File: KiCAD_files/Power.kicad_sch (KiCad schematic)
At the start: 44 parts, among them J101 Wago 6 contacts, P101 Power2, U101 AMC1311, U102 MCP6486UT-E/LT, U103 MCP6486UT-E/LT, U104 ACS723LLCTR-20AB

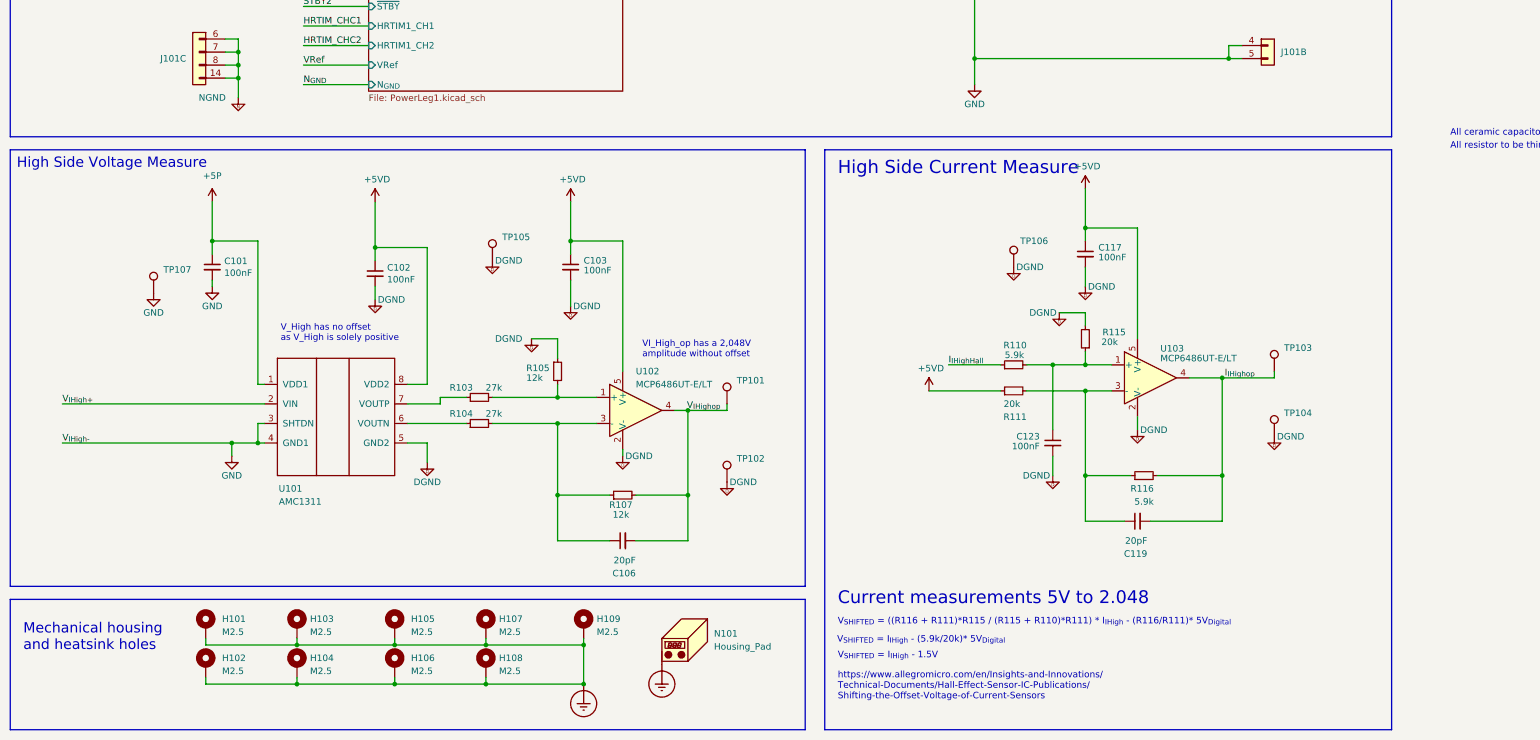
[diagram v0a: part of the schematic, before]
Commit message: better comments for VHigh conditionning signal
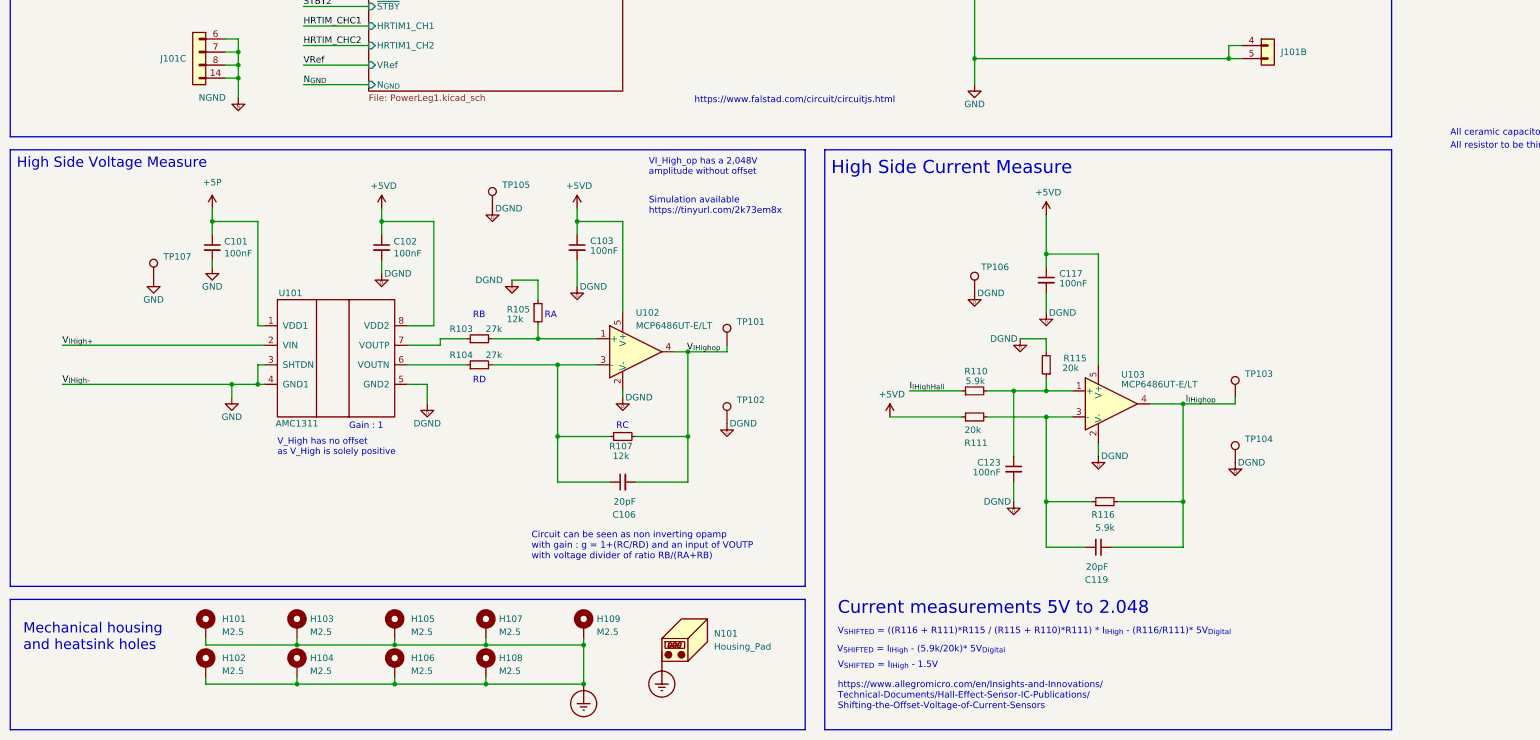
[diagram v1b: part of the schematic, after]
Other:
- note added: "Circuit can be seen as non inverting opamp with gain : g = 1+(RC/RD) and an input of VOUTP with voltage divider of ratio RB/(RA+RB)"
- note added: "Gain : 1"
- note added: "RA"
- note added: "RB"
- note added: "RC"
- note added: "RD"
- note added: "Simulation available https://tinyurl.com/2k73em8x"
- note added: "https://www.falstad.com/circuit/circuitjs.html"
- moved on the sheet: C101, C102, C103, C106, C117, C119, C123, R103, R104, R105, R107, R110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

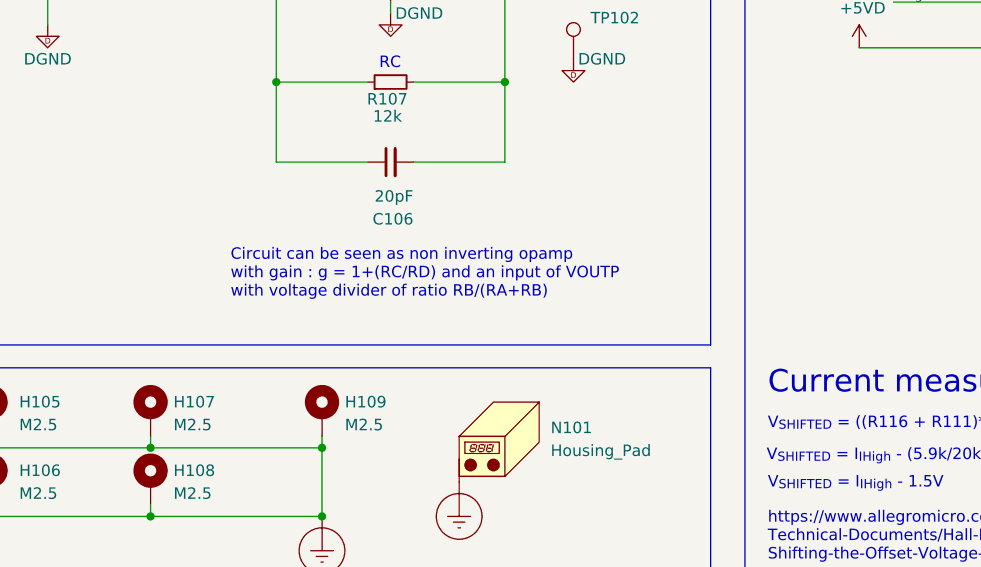
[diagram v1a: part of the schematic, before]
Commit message: more details for VLow conditionning
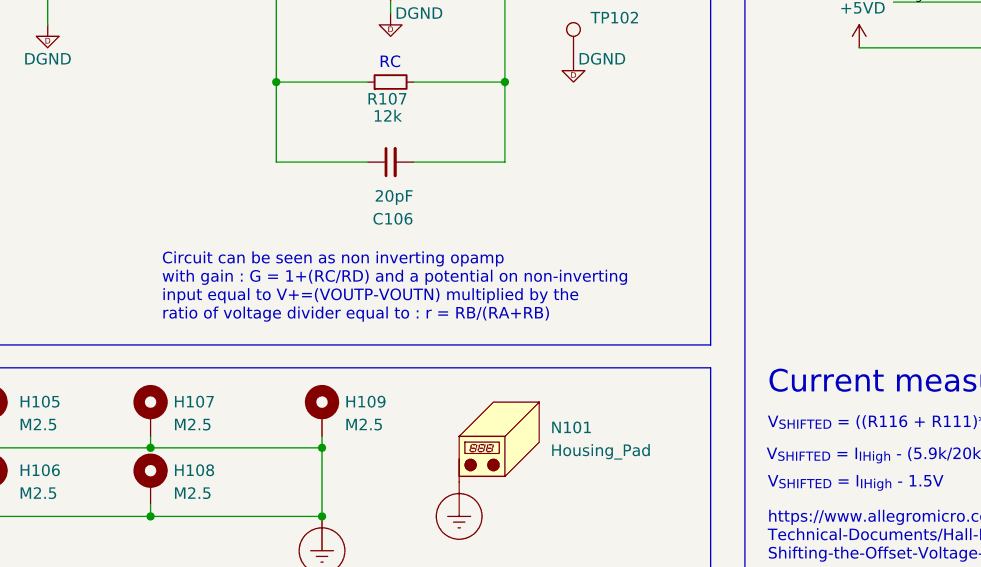
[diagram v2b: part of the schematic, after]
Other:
- note added: "Circuit can be seen as non inverting opamp with gain : G = 1+(RC/RD) and a potential on non-inverting input equal to V+=(VOUTP-VOUTN) multiplied by the ratio of voltage divider equal to : r = RB/(RA+RB)"
- note removed: "Circuit can be seen as non inverting opamp with gain : g = 1+(RC/RD) and an input of VOUTP with voltage divider of ratio RB/(RA+RB)"
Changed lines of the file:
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@@
     (effects (font (size 1.2446 1.2446)) (justify left bottom))
   )
-  (text "Circuit can be seen as non inverting opamp\nwith gain : g = 1+(RC/RD) and an input of VOUTP \nwith voltage divider of ratio RB/(RA+RB)"
-    (at 123.19 248.92 0)
+  (text "Circuit can be seen as non inverting opamp\nwith gain : G = 1+(RC/RD) and a potential on non-inverting\ninput equal to V+=(VOUTP-VOUTN) multiplied by the\nratio of voltage divider equal to : r = RB/(RA+RB)"
+    (at 115.57 251.46 0)
     (effects (font (size 1.27 1.27)) (justify left bottom))
   )

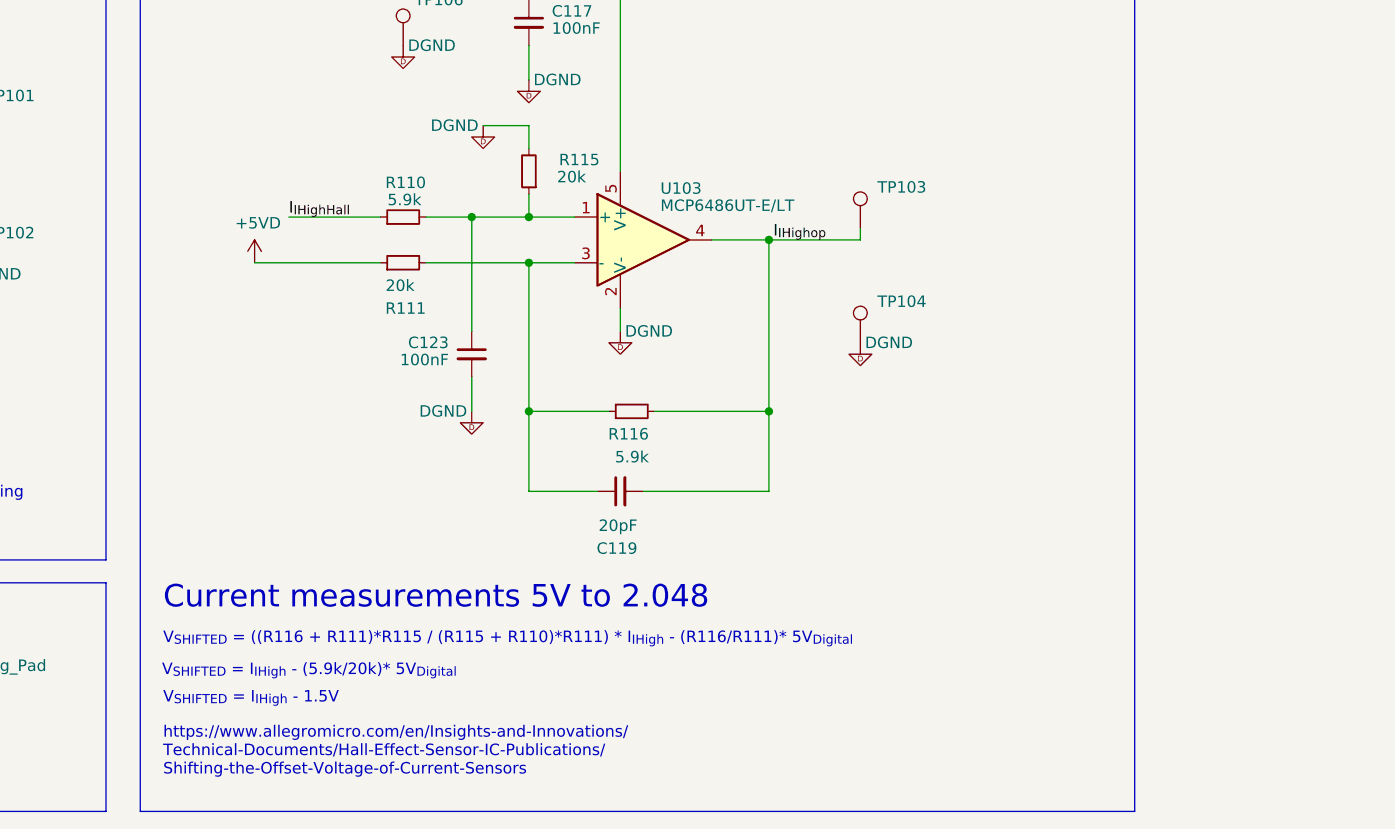
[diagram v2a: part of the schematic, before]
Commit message: better comments for current conditionning
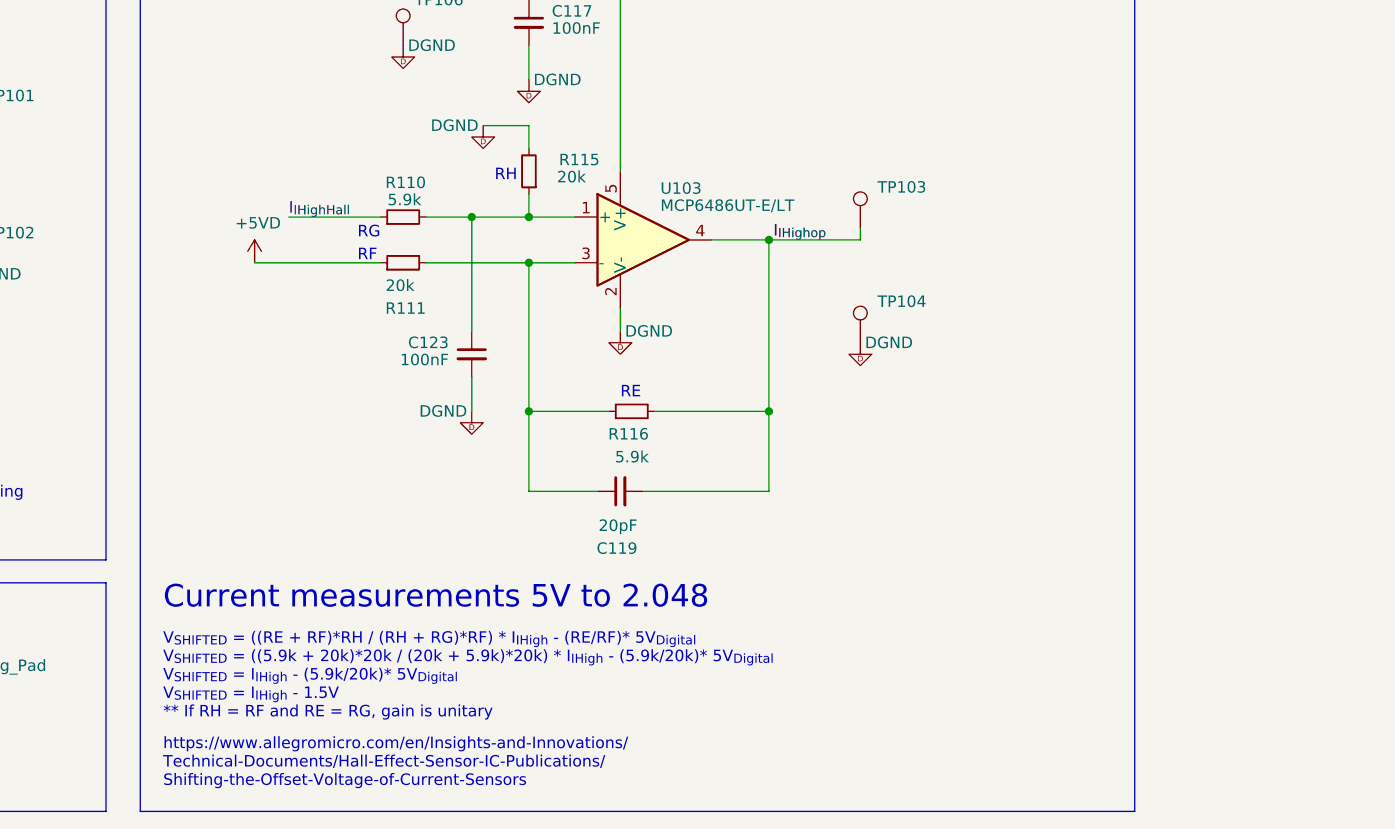
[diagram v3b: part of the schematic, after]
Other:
- note added: "RE"
- note added: "RF"
- note added: "RG"
- note added: "RH"
- note added: "V_{SHIFTED} = ((RE + RF)*RH / (RH + RG)*RF) * I_{IHigh} - (RE/RF)* 5V_{Digital} V_{SHIFTED} = ((5.9k + 20k)*20k / (20k + 5.9k)*20k) * I_{IHigh} - (5.9k/20k)* 5V_{Digital} V_{SHIFTED} = I_{IHigh} - (5.9k/20k)* 5V_{Digital} V_{SHIFTED} = I_{IHigh} - 1.5V ** If RH = RF and RE = RG, gain is unitary"
- note removed: "V_{SHIFTED} = ((R116 + R111)*R115 / (R115 + R110)*R111) * I_{IHigh} - (R116/R111)* 5V_{Digital}"
- note removed: "V_{SHIFTED} = I_{IHigh} - (5.9k/20k)* 5V_{Digital}"
- note removed: "V_{SHIFTED} = I_{IHigh} - 1.5V"
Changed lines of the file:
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@@
     (fill (type none))
+  )
+  (text "RG" (at 204.47 218.44 0)
+    (effects (font (size 1.27 1.27)) (justify left bottom))
   )
   (text "Contains the onboard power supply\nthat permits power converter blackstart\n"
@@
   )
   (text "https://www.allegromicro.com/en/Insights-and-Innovations/\nTechnical-Documents/Hall-Effect-Sensor-IC-Publications/\nShifting-the-Offset-Voltage-of-Current-Sensors"
-    (at 182.88 278.13 0)
-    (effects (font (size 1.27 1.27)) (justify left bottom))
-  )
-  (text "V_{SHIFTED} = I_{IHigh} - 1.5V\n" (at 182.88 270.129 0)
+    (at 182.88 279.4 0)
     (effects (font (size 1.27 1.27)) (justify left bottom))
   )
@@
   )
   (text "High side current sensor" (at 207.01 29.21 0)
-    (effects (font (size 1.27 1.27)) (justify left bottom))
-  )
-  (text "V_{SHIFTED} = I_{IHigh} - (5.9k/20k)* 5V_{Digital}"
-    (at 182.753 267.081 0)
     (effects (font (size 1.27 1.27)) (justify left bottom))
   )
@@
     (effects (font (size 3.5 3.5)) (justify left bottom))
   )
-  (text "V_{SHIFTED} = ((R116 + R111)*R115 / (R115 + R110)*R111) * I_{IHigh} - (R116/R111)* 5V_{Digital}"
-    (at 182.88 263.525 0)
+  (text "V_{SHIFTED} = ((RE + RF)*RH / (RH + RG)*RF) * I_{IHigh} - (RE/RF)* 5V_{Digital}\nV_{SHIFTED} = ((5.9k + 20k)*20k / (20k + 5.9k)*20k) * I_{IHigh} - (5.9k/20k)* 5V_{Digital}\nV_{SHIFTED} = I_{IHigh} - (5.9k/20k)* 5V_{Digital}\nV_{SHIFTED} = I_{IHigh} - 1.5V\n** If RH = RF and RE = RG, gain is unitary\n"
+    (at 182.88 271.78 0)
     (effects (font (size 1.27 1.27)) (justify left bottom))
   )
@@
     (effects (font (size 1.27 1.27)) (justify left bottom))
   )
+  (text "RE" (at 233.68 236.22 0)
+    (effects (font (size 1.27 1.27)) (justify left bottom))
+  )
+  (text "RF" (at 204.47 220.98 0)
+    (effects (font (size 1.27 1.27)) (justify left bottom))
+  )
   (text "Power Leg 2\n" (at 101.6 127 0)
     (effects (font (size 3.5 3.5)) (justify left bottom))
   )
+  (text "RH" (at 219.71 212.09 0)
+    (effects (font (size 1.27 1.27)) (justify left bottom))
+  )
   (text "Feeder " (at 337.82 111.76 0)

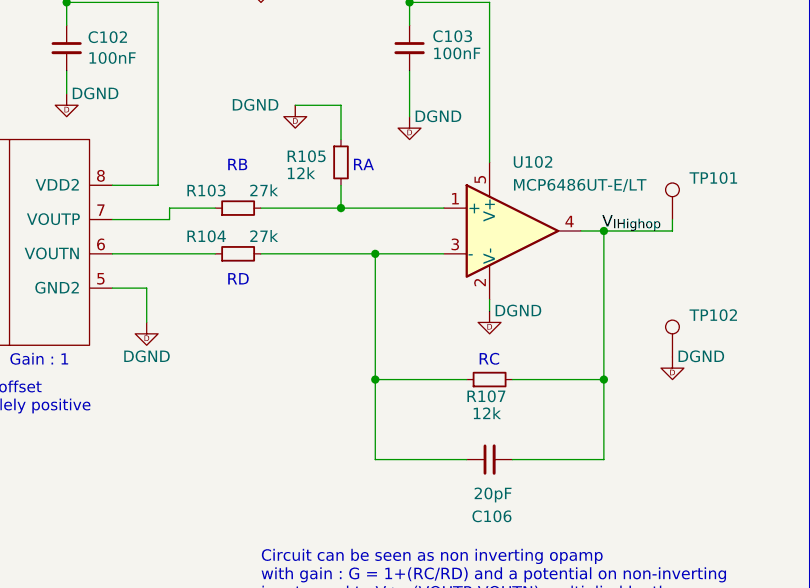
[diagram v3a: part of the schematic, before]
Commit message: R105 and R107 are now 27k for unitgain
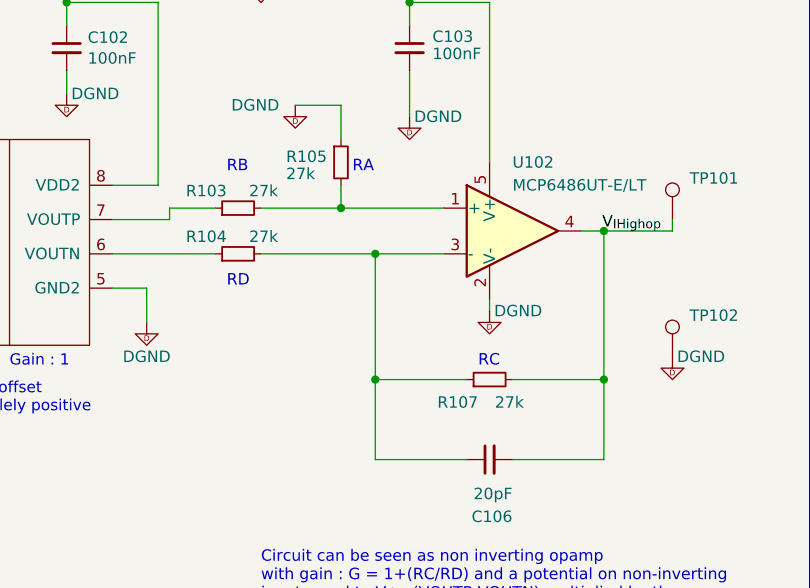
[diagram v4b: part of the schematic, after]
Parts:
- R105, R107: value 12k -> 27k; manf# CR0805-FX-1202ELF -> CR0805-FX-2702ELF
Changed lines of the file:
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@@
       (effects (font (size 1.27 1.27)) (justify left))
     )
-    (property "Value" "12k" (at 118.364 201.93 0)
+    (property "Value" "27k" (at 118.364 201.93 0)
       (effects (font (size 1.27 1.27)) (justify left))
     )
@@
       (effects (font (size 1.27 1.27)) hide)
     )
-    (property "manf#" "CR0805-FX-1202ELF" (at 124.46 200.66 0)
+    (property "manf#" "CR0805-FX-2702ELF" (at 124.46 200.66 0)
       (effects (font (size 1.27 1.27)) hide)
     )
@@
         (path "/8d0c1d66-35ef-4a53-a28f-436a11b54f42"
           (reference "R105") (unit 1)
-        )
-      )
-    )
-  )
-  (symbol (lib_id "Device:R_Small") (at 140.97 224.79 90) (unit 1)
-    (in_bom yes) (on_board yes) (dnp no)
-    (property "Reference" "R107" (at 142.875 226.695 90)
-      (effects (font (size 1.27 1.27)) (justify left))
-    )
-    (property "Value" "12k" (at 142.24 228.6 90)
-      (effects (font (size 1.27 1.27)) (justify left))
-    )
-    (property "Footprint" "Footprints:R_0805_2012Metric" (at 140.97 224.79 0)
-      (effects (font (size 1.27 1.27)) hide)
-    )
-    (property "Datasheet" "~" (at 140.97 224.79 0)
-      (effects (font (size 1.27 1.27)) hide)
-    )
-    (property "manf#" "CR0805-FX-1202ELF" (at 140.97 224.79 0)
-      (effects (font (size 1.27 1.27)) hide)
-    )
-    (property "Functional Block" "Measurement" (at 140.97 224.79 0)
-      (effects (font (size 1.27 1.27)) hide)
-    )
-    (property "Metal content" "NiCr" (at 140.97 224.79 0)
-      (effects (font (size 1.27 1.27)) hide)
-    )
-    (property "Subfunction" "VIHigh measure" (at 140.97 224.79 0)
-      (effects (font (size 1.27 1.27)) hide)
-    )
-    (pin "1")
-    (pin "2")
-    (instances
-      (project "Power"
-        (path "/8d0c1d66-35ef-4a53-a28f-436a11b54f42"
-          (reference "R107") (unit 1)
         )
       )
@@
         )
       )
+    )
+  )
+  (symbol (lib_name "R_Small_14") (lib_id "Device:R_Small") (at 140.97 224.79 90) (unit 1)
+    (in_bom yes) (on_board yes) (dnp no)
+    (property "Reference" "R107" (at 139.7 227.33 90)
+      (effects (font (size 1.27 1.27)) (justify left))
+    )
+    (property "Value" "27k" (at 144.78 227.33 90)
+      (effects (font (size 1.27 1.27)) (justify left))
+    )
+    (property "Footprint" "Footprints:R_0805_2012Metric" (at 140.97 224.79 0)
+      (effects (font (size 1.27 1.27)) hide)
+    )
+    (property "Datasheet" "~" (at 140.97 224.79 0)
+      (effects (font (size 1.27 1.27)) hide)
+    )
+    (property "manf#" "CR0805-FX-2702ELF" (at 140.97 224.79 0)
+      (effects (font (size 1.27 1.27)) hide)
+    )
+    (property "Functional Block" "Measurement" (at 140.97 224.79 0)
+      (effects (font (size 1.27 1.27)) hide)
+    )
+    (property "Metal content" "NiCr" (at 140.97 224.79 0)
+      (effects (font (size 1.27 1.27)) hide)
+    )
+    (property "Subfunction" "VIHigh measure" (at 140.97 224.79 0)
+      (effects (font (size 1.27 1.27)) hide)
+    )
+    (pin "1")
+    (pin "2")
+    (instances
+      (project "Power"
+        (path "/8d0c1d66-35ef-4a53-a28f-436a11b54f42"
+          (reference "R107") (unit 1)
+        )
+      )
